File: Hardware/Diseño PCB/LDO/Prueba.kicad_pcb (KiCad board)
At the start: 2 copper layers, 98.5 x 100.5 mm, 55 parts, among them Q1 2N3904, Q10 BC557, Q11 BC547, Q12 BC557, Q13 BC557, Q14 BC547, Q15 BC557, Q16 BC547, Q17 BC557, Q18 BC547, Q19 BC547, Q2 BC547, Q3 BC547, Q4 BC557, Q5 BC557, Q6 BC547, Q7 BC547, Q8 IRF4905, Q9 BC547, U1 TL431LP, U4 LM324

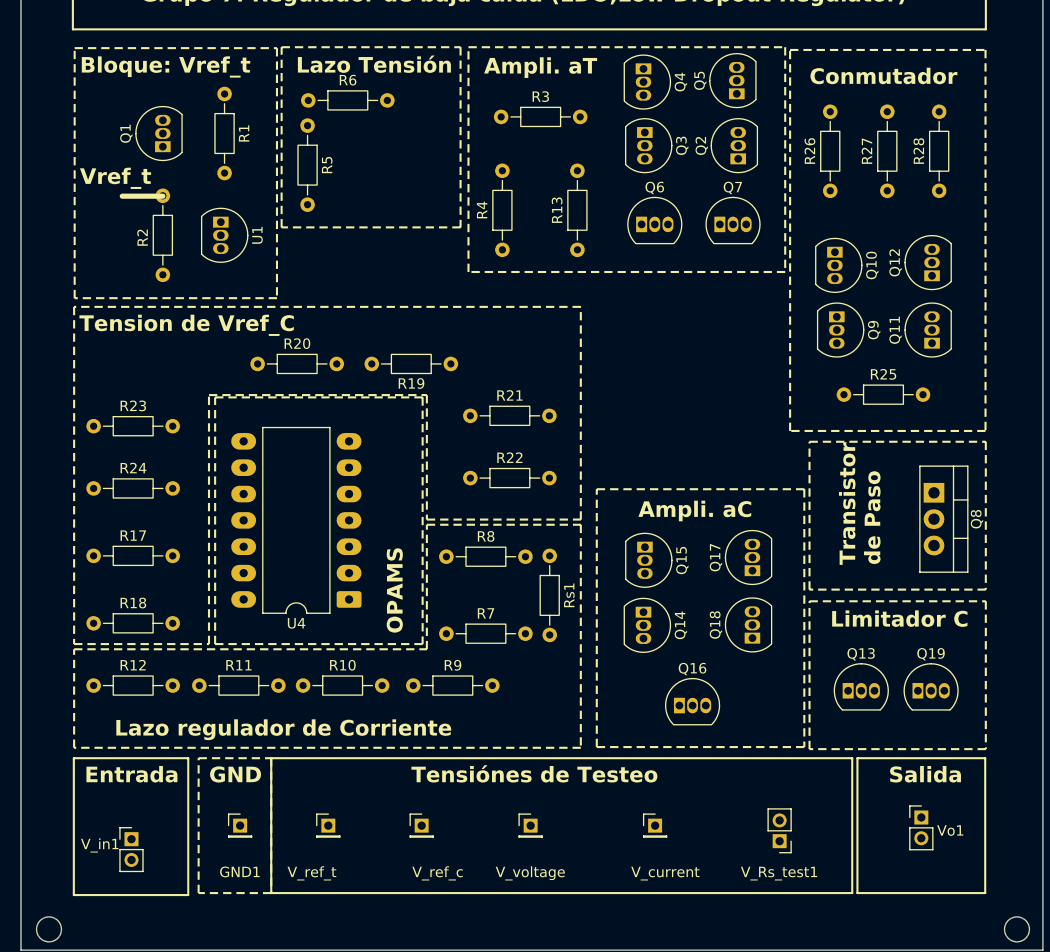
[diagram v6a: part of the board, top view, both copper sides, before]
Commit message: Diseño PCB: Pistas y C compensacion en Pcb
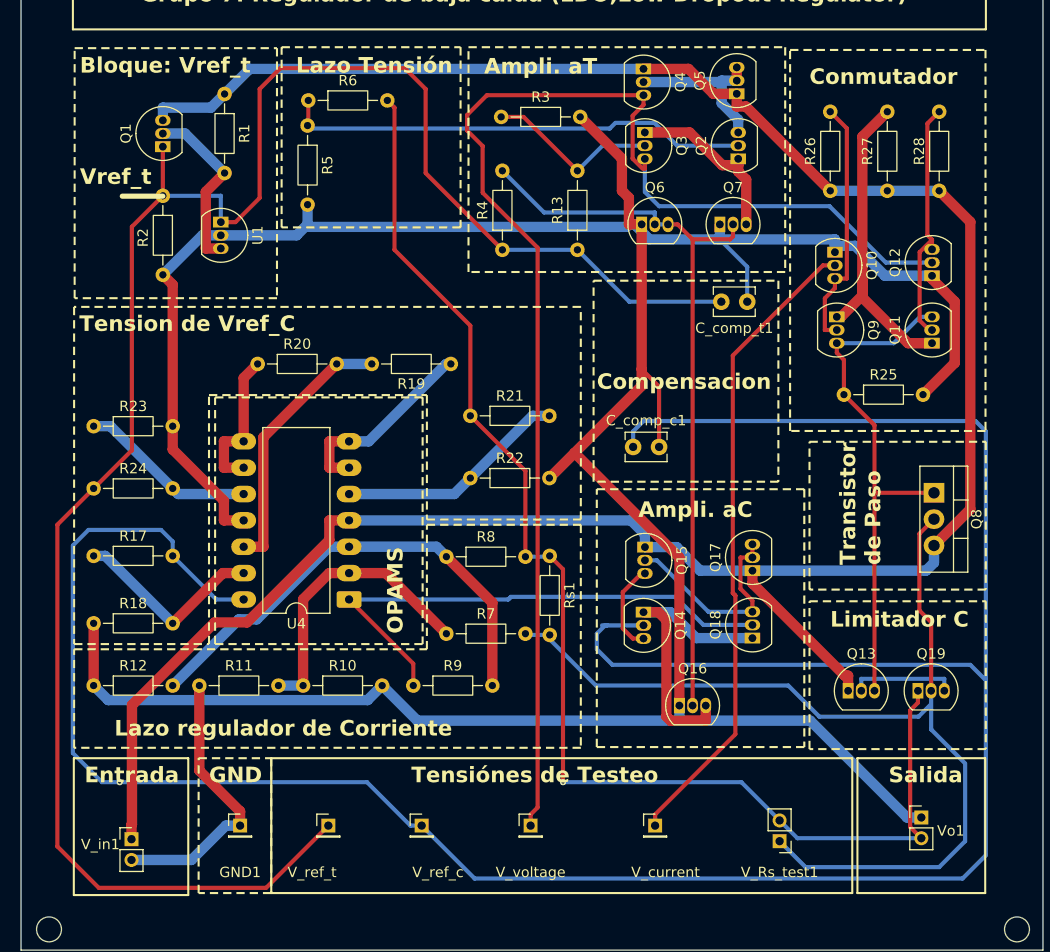
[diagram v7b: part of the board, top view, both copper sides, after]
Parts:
- added C_comp_c1: 220 nF, Capacitor_THT:C_Disc_D3.8mm_W2.6mm_P2.50mm, F.Cu at (158.0, 98.0)
- added C_comp_t1: 100 pF, Capacitor_THT:C_Disc_D3.8mm_W2.6mm_P2.50mm, F.Cu at (169.0, 84.0)
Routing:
- net GND: track 0.00 -> 332.6 mm
- net Vref_c: track 0.00 -> 257.4 mm, vias 0 -> 1
- net Vcc: track 0.00 -> 239.1 mm
- net Vref: track 0.00 -> 184.6 mm
- net V_voltage: track 0.00 -> 132.1 mm
- net -V_Rs: track 0.00 -> 126.0 mm, vias 0 -> 1
- net +V_Rs: track 0.00 -> 96.6 mm
- net nodo A: track 0.00 -> 71.8 mm
- net V_current_ref: track 0.00 -> 62.4 mm
- net VF_fa: track 0.00 -> 51.3 mm
- net Vctrl: track 0.00 -> 51.0 mm
- net Net-(U4A-+): track 0.00 -> 46.6 mm
- net VF_fv: track 0.00 -> 45.2 mm
- net Net-(Q11-C): track 0.00 -> 32.2 mm
- net Net-(Q14-E): track 0.00 -> 28.8 mm
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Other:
- board text added: "Compensacion"

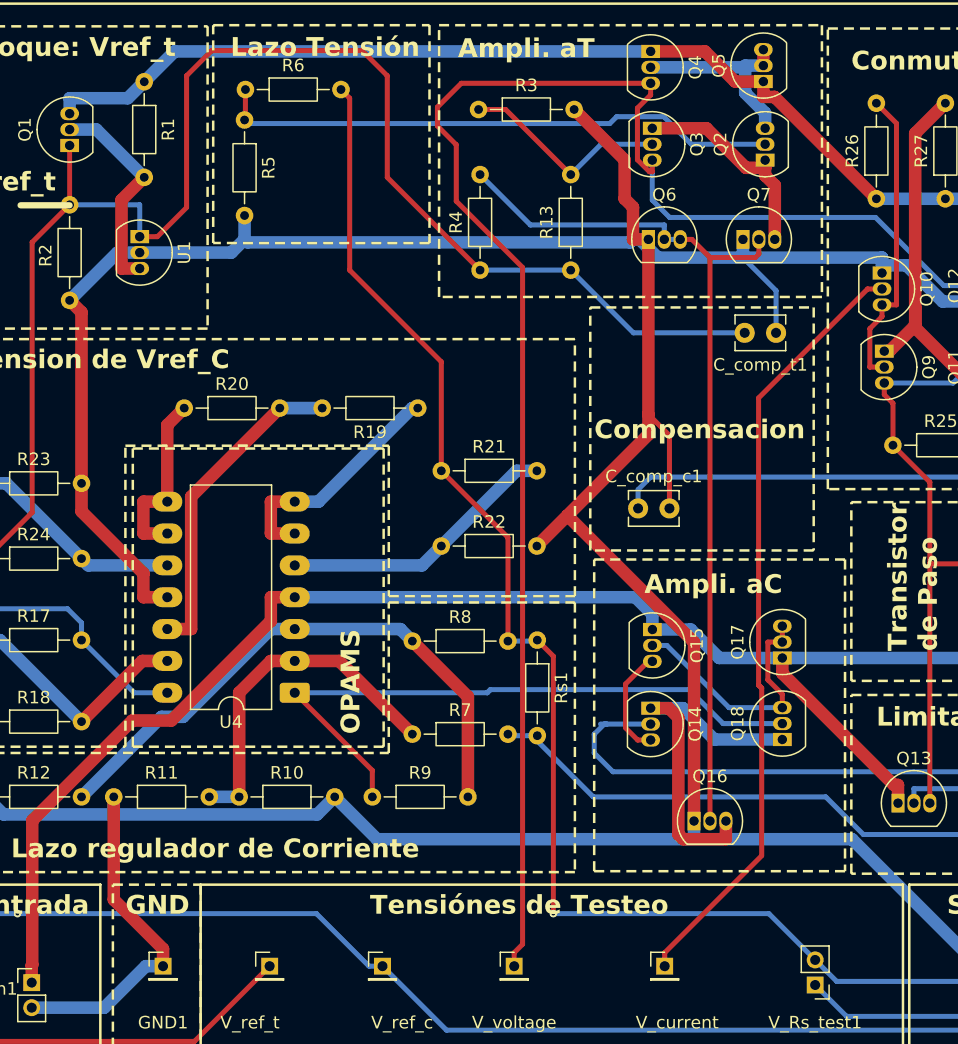
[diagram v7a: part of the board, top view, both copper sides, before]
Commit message: Diseño PCB: Pistas y C compensacion en Pcb
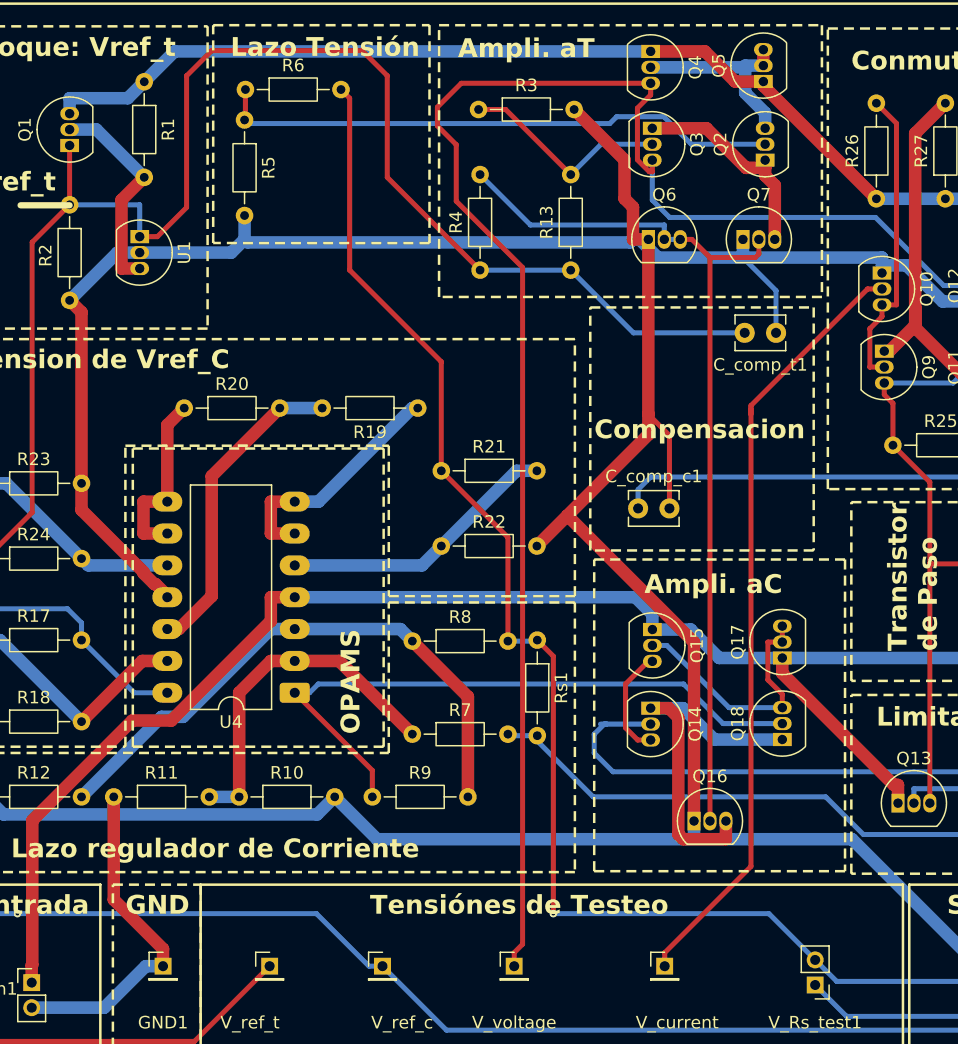
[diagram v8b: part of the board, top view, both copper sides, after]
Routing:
- net GND: track 332.6 -> 331.5 mm
- net Net-(U4D-+): track 25.8 -> 25.3 mm
- net Vcc: track 239.1 -> 238.6 mm
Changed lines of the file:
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@@
+	)
+	(segment
+		(start 167.99 64.3)
+		(end 167.99 63.96)
+		(width 1)
+		(layer "F.Cu")
+		(net "Vcc")
 	)
 	(segment
@@
 	)
 	(segment
-		(start 167.99 63.96)
-		(end 167.99 65.1867)
+		(start 177 73.31)
+		(end 167.99 64.3)
 		(width 1)
 		(layer "F.Cu")
@@
 	)
 	(segment
-		(start 177 73.31)
-		(end 168.8767 65.1867)
-		(width 1)
-		(layer "F.Cu")
-		(net "Vcc")
-	)
-	(segment
 		(start 130.62 105.08)
 		(end 128.7183 105.08)
@@
 	)
 	(segment
-		(start 168.8767 65.1867)
-		(end 167.99 65.1867)
-		(width 1)
-		(layer "F.Cu")
-		(net "Vcc")
-	)
-	(segment
 		(start 163.333 61.56)
 		(end 159 61.56)
@@
 	)
 	(segment
-		(start 120.46 105.08)
-		(end 118.5583 105.08)
-		(width 1)
-		(layer "F.Cu")
-		(net "GND")
-	)
-	(segment
 		(start 157.5933 76.55)
 		(end 157.5933 73.9785)
@@
 	)
 	(segment
+		(start 120.46 104.96)
+		(end 119.54 104.04)
+		(width 1)
+		(layer "F.Cu")
+		(net "GND")
+	)
+	(segment
 		(start 106 121)
 		(end 106 115)
@@
 	)
 	(segment
-		(start 118.5583 105.08)
-		(end 118.5583 103.1783)
+		(start 119.43868 104.04)
+		(end 118.56 103.16132)
 		(width 1)
 		(layer "F.Cu")
@@
 	)
 	(segment
+		(start 120.46 105.08)
+		(end 120.46 104.96)
+		(width 1)
+		(layer "F.Cu")
+		(net "GND")
+	)
+	(segment
 		(start 156.9206 73.3058)
 		(end 156.9206 70.2106)
@@
 	)
 	(segment
+		(start 113.62 98.12)
+		(end 113.62 96)
+		(width 1)
+		(layer "F.Cu")
+		(net "GND")
+	)
+	(segment
 		(start 162.46 108.6683)
 		(end 152.3609 98.5691)
@@
 	)
 	(segment
+		(start 118.56 103.16132)
+		(end 118.56 103.06)
+		(width 1)
+		(layer "F.Cu")
+		(net "GND")
+	)
+	(segment
 		(start 160.5 98)
 		(end 160.5 92.18)
@@
 	)
 	(segment
+		(start 118.56 103.06)
+		(end 113.62 98.12)
+		(width 1)
+		(layer "F.Cu")
+		(net "GND")
+	)
+	(segment
 		(start 116.19 121)
 		(end 116.19 129.1933)
@@
 	)
 	(segment
-		(start 118.5583 103.1783)
-		(end 113.62 98.24)
-		(width 1)
-		(layer "F.Cu")
-		(net "GND")
-	)
-	(segment
-		(start 113.62 98.24)
-		(end 113.62 96)
+		(start 119.54 104.04)
+		(end 119.43868 104.04)
 		(width 1)
 		(layer "F.Cu")
@@
 	)
 	(segment
-		(start 162.073 112.4509)
-		(end 146.2181 112.4509)
-		(width 0.4)
-		(layer "B.Cu")
-		(net "VF_fa")
-	)
-	(segment
 		(start 130.6215 112.6985)
 		(end 130.62 112.7)
@@
 	(segment
 		(start 164.7779 115.1558)
-		(end 162.073 112.4509)
+		(end 161.6221 112)
+		(width 0.4)
+		(layer "B.Cu")
+		(net "VF_fa")
+	)
+	(segment
+		(start 161.6221 112)
+		(end 132.5 112)
 		(width 0.4)
 		(layer "B.Cu")
@@
 	)
 	(segment
-		(start 146.2181 112.4509)
-		(end 145.9705 112.6985)
+		(start 131.8015 112.6985)
+		(end 130.6215 112.6985)
 		(width 0.4)
 		(layer "B.Cu")
@@
 	)
 	(segment
-		(start 145.9705 112.6985)
-		(end 130.6215 112.6985)
-		(width 0.4)
-		(layer "B.Cu")
-		(net "VF_fa")
-	)
-	(segment
-		(start 146.2181 112.4509)
-		(end 145.9705 112.6985)
+		(start 132.5 112)
+		(end 131.8015 112.6985)
 		(width 0.4)
 		(layer "B.Cu")
@@
 	)
 	(segment
-		(start 120.46 107.62)
-		(end 122.3617 107.62)
+		(start 129.43 90)
+		(end 124 95.43)
 		(width 1)
 		(layer "F.Cu")
@@
 	)
 	(segment
-		(start 122.3617 97.0683)
-		(end 122.3617 107.62)
+		(start 121.38 107.62)
+		(end 120.46 107.62)
 		(width 1)
 		(layer "F.Cu")
@@
 	)
 	(segment
-		(start 129.43 90)
-		(end 122.3617 97.0683)
+		(start 124 95.43)
+		(end 124 105)
+		(width 1)
+		(layer "F.Cu")
+		(net "Net-(U4D-+)")
+	)
+	(segment
+		(start 124 105)
+		(end 121.38 107.62)
 		(width 1)
 		(layer "F.Cu")
@@
 	)
 	(segment
+		(start 167 126.5433)
+		(end 160.12 133.4233)
+		(width 0.4)
+		(layer "F.Cu")
+		(net "V_current_ref")
+	)
+	(segment
+		(start 167 90)
+		(end 167 126.5433)
+		(width 0.4)
+		(layer "F.Cu")
+		(net "V_current_ref")
+	)
+	(segment
+		(start 167 89.7983)
+		(end 167 90.5)
+		(width 0.4)
+		(layer "F.Cu")
+		(net "V_current_ref")
+	)
+	(segment
 		(start 177.45 80.5)
 		(end 176.2983 80.5)
@@
 	)
 	(segment
-		(start 160.12 134.5)
-		(end 160.12 133.4233)
+		(start 160.12 133.4233)
+		(end 160.12 134.5)
 		(width 0.4)
 		(layer "F.Cu")
@@
 	)
 	(segment
-		(start 167.8539 112.3248)
-		(end 167.8539 125.6894)
-		(width 0.4)
-		(layer "F.Cu")
-		(net "V_current_ref")
-	)
-	(segment
-		(start 167.6048 112.0757)
-		(end 167.8539 112.3248)
-		(width 0.4)
-		(layer "F.Cu")
-		(net "V_current_ref")
-	)
-	(segment
-		(start 167.8539 125.6894)
-		(end 160.12 133.4233)
-		(width 0.4)
-		(layer "F.Cu")
-		(net "V_current_ref")
-	)
-	(segment
-		(start 167.6048 89.1935)
-		(end 167.6048 112.0757)
-		(width 0.4)
-		(layer "F.Cu")
-		(net "V_current_ref")
-	)
-	(segment
 		(start 176.2983 80.5)
-		(end 167.6048 89.1935)
-		(width 0.4)
-		(layer "F.Cu")
-		(net "V_current_ref")
-	)
-	(segment
-		(start 167.6048 112.0757)
-		(end 167.8539 112.3248)
-		(width 0.4)
-		(layer "F.Cu")
+		(end 167 89.7983)
+		(width 0.4)
+		(layer "F.Cu")
